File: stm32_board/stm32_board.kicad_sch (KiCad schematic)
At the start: 10 parts, among them U1 STM32F103C8Tx

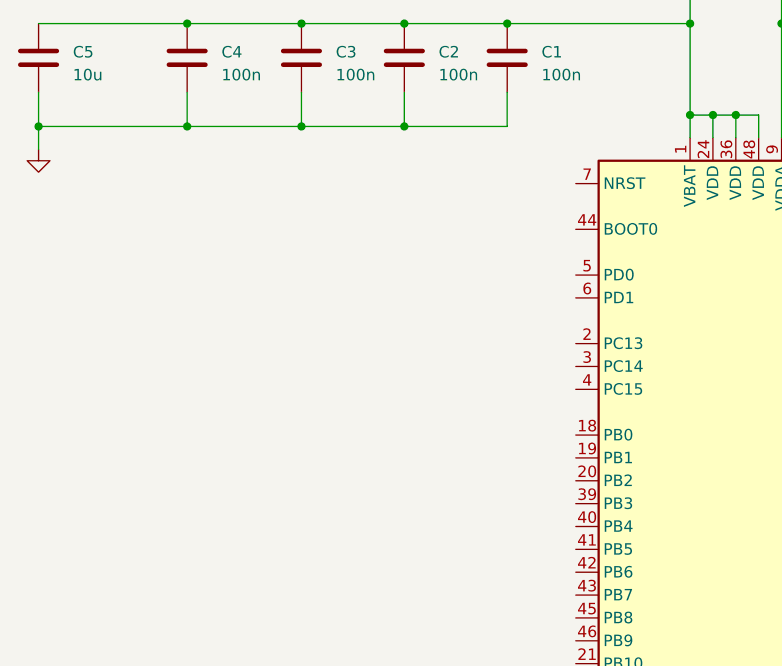
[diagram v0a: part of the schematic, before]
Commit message: Added Bootloader switch
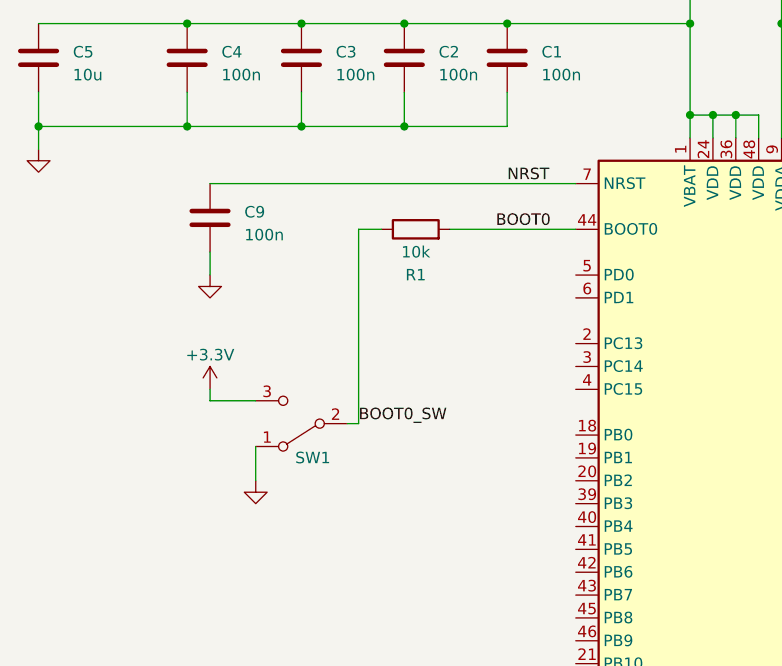
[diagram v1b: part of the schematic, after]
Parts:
- added C9: 100n, symbol Device:C
- added R1: 10k, symbol Device:R
- added SW1: SW_SPDT, symbol Switch:SW_SPDT
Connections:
- net +3.3V: now also SW1.3 (C)
- net GND: now also C9.2, SW1.1 (A)
- net BOOT0: now reaches U1.44 (BOOT0)
- net BOOT0: now also R1.2
- net NRST: now reaches U1.7 (NRST)
- net NRST: now also C9.1
- new net BOOT0_SW: R1.1, SW1.2 (B)
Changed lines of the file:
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@@
+    (stroke (width 0) (type default))
+  )
+  (wire (pts (xy 111.76 86.36) (xy 110.49 86.36))
     (stroke (width 0) (type default))
   )
@@
     (stroke (width 0) (type default))
   )
+  (wire (pts (xy 100.33 88.9) (xy 100.33 92.71))
+    (stroke (width 0) (type default))
+  )
   (wire (pts (xy 189.23 52.07) (xy 189.23 55.88))
     (stroke (width 0) (type default))
@@
     (stroke (width 0) (type default))
   )
+  (wire (pts (xy 121.92 64.77) (xy 135.89 64.77))
+    (stroke (width 0) (type default))
+  )
   (wire (pts (xy 116.84 49.53) (xy 116.84 53.34))
     (stroke (width 0) (type default))
   )
+  (wire (pts (xy 111.76 86.36) (xy 111.76 64.77))
+    (stroke (width 0) (type default))
+  )
   (wire (pts (xy 92.71 41.91) (xy 105.41 41.91))
     (stroke (width 0) (type default))
@@
     (stroke (width 0) (type default))
   )
+  (wire (pts (xy 95.25 67.31) (xy 95.25 69.85))
+    (stroke (width 0) (type default))
+  )
   (wire (pts (xy 76.2 53.34) (xy 76.2 55.88))
     (stroke (width 0) (type default))
@@
     (stroke (width 0) (type default))
   )
+  (wire (pts (xy 111.76 64.77) (xy 114.3 64.77))
+    (stroke (width 0) (type default))
+  )
   (wire (pts (xy 148.59 36.83) (xy 148.59 41.91))
     (stroke (width 0) (type default))
@@
     (stroke (width 0) (type default))
   )
+  (wire (pts (xy 100.33 83.82) (xy 95.25 83.82))
+    (stroke (width 0) (type default))
+  )
   (wire (pts (xy 148.59 41.91) (xy 148.59 52.07))
     (stroke (width 0) (type default))
   )
+  (wire (pts (xy 95.25 59.69) (xy 135.89 59.69))
+    (stroke (width 0) (type default))
+  )
   (wire (pts (xy 92.71 49.53) (xy 92.71 53.34))
     (stroke (width 0) (type default))
@@
     (stroke (width 0) (type default))
   )
+  (wire (pts (xy 95.25 83.82) (xy 95.25 82.55))
+    (stroke (width 0) (type default))
+  )
   (wire (pts (xy 128.27 41.91) (xy 148.59 41.91))
     (stroke (width 0) (type default))
@@
   (wire (pts (xy 76.2 53.34) (xy 92.71 53.34))
     (stroke (width 0) (type default))
+  )
+  (label "BOOT0" (at 127 64.77 0) (fields_autoplaced)
+    (effects (font (size 1.27 1.27)) (justify left bottom))
+  )
+  (label "NRST" (at 128.27 59.69 0) (fields_autoplaced)
+    (effects (font (size 1.27 1.27)) (justify left bottom))
+  )
+  (label "BOOT0_SW" (at 111.76 86.36 0) (fields_autoplaced)
+    (effects (font (size 1.27 1.27)) (justify left bottom))
+  )
+  (symbol (lib_id "power:GND") (at 100.33 92.71 0) (unit 1)
+    (in_bom yes) (on_board yes) (dnp no) (fields_autoplaced)
+    (property "Reference" "#PWR09" (at 100.33 99.06 0)
+      (effects (font (size 1.27 1.27)) hide)
+    )
+    (property "Value" "GND" (at 100.33 97.79 0)
+      (effects (font (size 1.27 1.27)) hide)
+    )
+    (property "Footprint" "" (at 100.33 92.71 0)
+      (effects (font (size 1.27 1.27)) hide)
+    )
+    (property "Datasheet" "" (at 100.33 92.71 0)
+      (effects (font (size 1.27 1.27)) hide)
+    )
+    (pin "1")
+    (instances
+      (project "stm32_board"
+        (path "/058edb5f-f5a5-4cac-aa4e-0bf18ffaa150"
+          (reference "#PWR09") (unit 1)
+        )
+      )
+    )
   )
   (symbol (lib_id "MCU_ST_STM32F1:STM32F103C8Tx") (at 151.13 95.25 0) (unit 1)
@@
     )
   )
+  (symbol (lib_id "Device:R") (at 118.11 64.77 90) (unit 1)
+    (in_bom yes) (on_board yes) (dnp no)
+    (property "Reference" "R1" (at 118.11 69.85 90)
+      (effects (font (size 1.27 1.27)))
+    )
+    (property "Value" "10k" (at 118.11 67.31 90)
+      (effects (font (size 1.27 1.27)))
+    )
+    (property "Footprint" "" (at 118.11 66.548 90)
+      (effects (font (size 1.27 1.27)) hide)
+    )
+    (property "Datasheet" "~" (at 118.11 64.77 0)
+      (effects (font (size 1.27 1.27)) hide)
+    )
+    (pin "1")
+    (pin "2")
+    (instances
+      (project "stm32_board"
+        (path "/058edb5f-f5a5-4cac-aa4e-0bf18ffaa150"
+          (reference "R1") (unit 1)
+        )
+      )
+    )
+  )
   (symbol (lib_id "power:GND") (at 189.23 55.88 0) (unit 1)
     (in_bom yes) (on_board yes) (dnp no) (fields_autoplaced)
@@
     )
   )
+  (symbol (lib_id "Switch:SW_SPDT") (at 105.41 86.36 180) (unit 1)
+    (in_bom yes) (on_board yes) (dnp no)
+    (property "Reference" "SW1" (at 106.68 90.17 0)
+      (effects (font (size 1.27 1.27)))
+    )
+    (property "Value" "SW_SPDT" (at 107.95 92.71 0)
+      (effects (font (size 1.27 1.27)) hide)
+    )
+    (property "Footprint" "" (at 105.41 86.36 0)
+      (effects (font (size 1.27 1.27)) hide)
+    )
+    (property "Datasheet" "~" (at 105.41 86.36 0)
+      (effects (font (size 1.27 1.27)) hide)
+    )
+    (pin "1")
+    (pin "2")
+    (pin "3")
+    (instances
+      (project "stm32_board"
+        (path "/058edb5f-f5a5-4cac-aa4e-0bf18ffaa150"
+          (reference "SW1") (unit 1)
+        )
+      )
+    )
+  )
   (symbol (lib_id "Device:C") (at 215.9 45.72 0) (unit 1)
     (in_bom yes) (on_board yes) (dnp no) (fields_autoplaced)
@@
     )
   )
+  (symbol (lib_id "power:GND") (at 95.25 69.85 0) (unit 1)
+    (in_bom yes) (on_board yes) (dnp no) (fields_autoplaced)
+    (property "Reference" "#PWR08" (at 95.25 76.2 0)
+      (effects (font (size 1.27 1.27)) hide)
+    )
+    (property "Value" "GND" (at 95.25 74.93 0)
+      (effects (font (size 1.27 1.27)) hide)
+    )
+    (property "Footprint" "" (at 95.25 69.85 0)
+      (effects (font (size 1.27 1.27)) hide)
+    )
+    (property "Datasheet" "" (at 95.25 69.85 0)
+      (effects (font (size 1.27 1.27)) hide)
+    )
+    (pin "1")
+    (instances
+      (project "stm32_board"
+        (path "/058edb5f-f5a5-4cac-aa4e-0bf18ffaa150"
+          (reference "#PWR08") (unit 1)
+        )
+      )
+    )
+  )
   (symbol (lib_id "Device:C") (at 189.23 45.72 0) (unit 1)
     (in_bom yes) (on_board yes) (dnp no) (fields_autoplaced)
@@
         (path "/058edb5f-f5a5-4cac-aa4e-0bf18ffaa150"
           (reference "#PWR03") (unit 1)
+        )
+      )
+    )
+  )
+  (symbol (lib_id "Device:C") (at 95.25 63.5 0) (unit 1)
+    (in_bom yes) (on_board yes) (dnp no) (fields_autoplaced)
+    (property "Reference" "C9" (at 99.06 62.865 0)
+      (effects (font (size 1.27 1.27)) (justify left))
+    )
+    (property "Value" "100n" (at 99.06 65.405 0)
+      (effects (font (size 1.27 1.27)) (justify left))
+    )
+    (property "Footprint" "" (at 96.2152 67.31 0)
+      (effects (font (size 1.27 1.27)) hide)
+    )
+    (property "Datasheet" "~" (at 95.25 63.5 0)
+      (effects (font (size 1.27 1.27)) hide)
+    )
+    (pin "1")
+    (pin "2")
+    (instances
+      (project "stm32_board"
+        (path "/058edb5f-f5a5-4cac-aa4e-0bf18ffaa150"
+          (reference "C9") (unit 1)
         )
       )
@@
         )
       )
+    )
+  )
+  (symbol (lib_id "power:+3.3V") (at 95.25 82.55 0) (unit 1)
+    (in_bom yes) (on_board yes) (dnp no)
+    (property "Reference" "#PWR010" (at 95.25 86.36 0)
+      (effects (font (size 1.27 1.27)) hide)
+    )
+    (property "Value" "+3.3V" (at 95.25 78.74 0)
+      (effects (font (size 1.27 1.27)))
+    )
+    (property "Footprint" "" (at 95.25 82.55 0)
+      (effects (font (size 1.27 1.27)) hide)
+    )
+    (property "Datasheet" "" (at 95.25 82.55 0)
+      (effects (font (size 1.27 1.27)) hide)
+    )
+    (pin "1")
+    (instances
+      (project "stm32_board"
+        (path "/058edb5f-f5a5-4cac-aa4e-0bf18ffaa150"
+          (reference "#PWR010") (unit 1)
+        )
+      )
